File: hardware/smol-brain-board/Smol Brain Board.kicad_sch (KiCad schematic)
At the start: 67 parts, among them J1 USB4085-GF-A, J12 Jumper 2Way Vert Solderable, J3 CAN_DBG, J5 Jumper 2Way Vert Solderable, J6 Smol_Brain_Board, J7 PROGRAM, J8 Jumper 2Way Vert Solderable, J9 Jumper 2Way Vert Solderable, U1 ESP32-S3-WROOM-1-N8, U3 SN65HVD231D

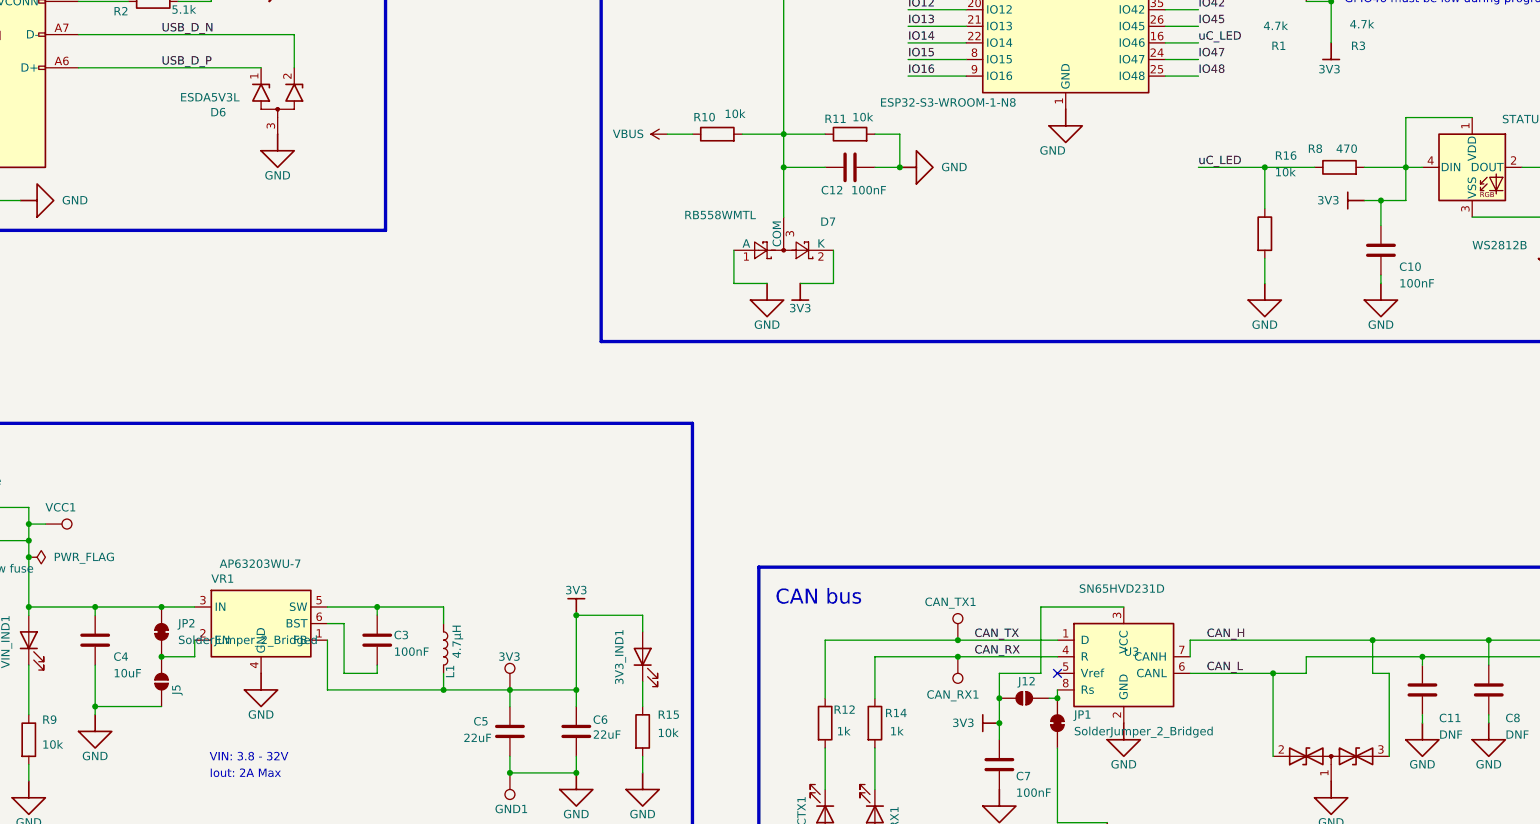
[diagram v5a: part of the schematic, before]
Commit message: Schematic fixes, foot print and crossovers, continued routing
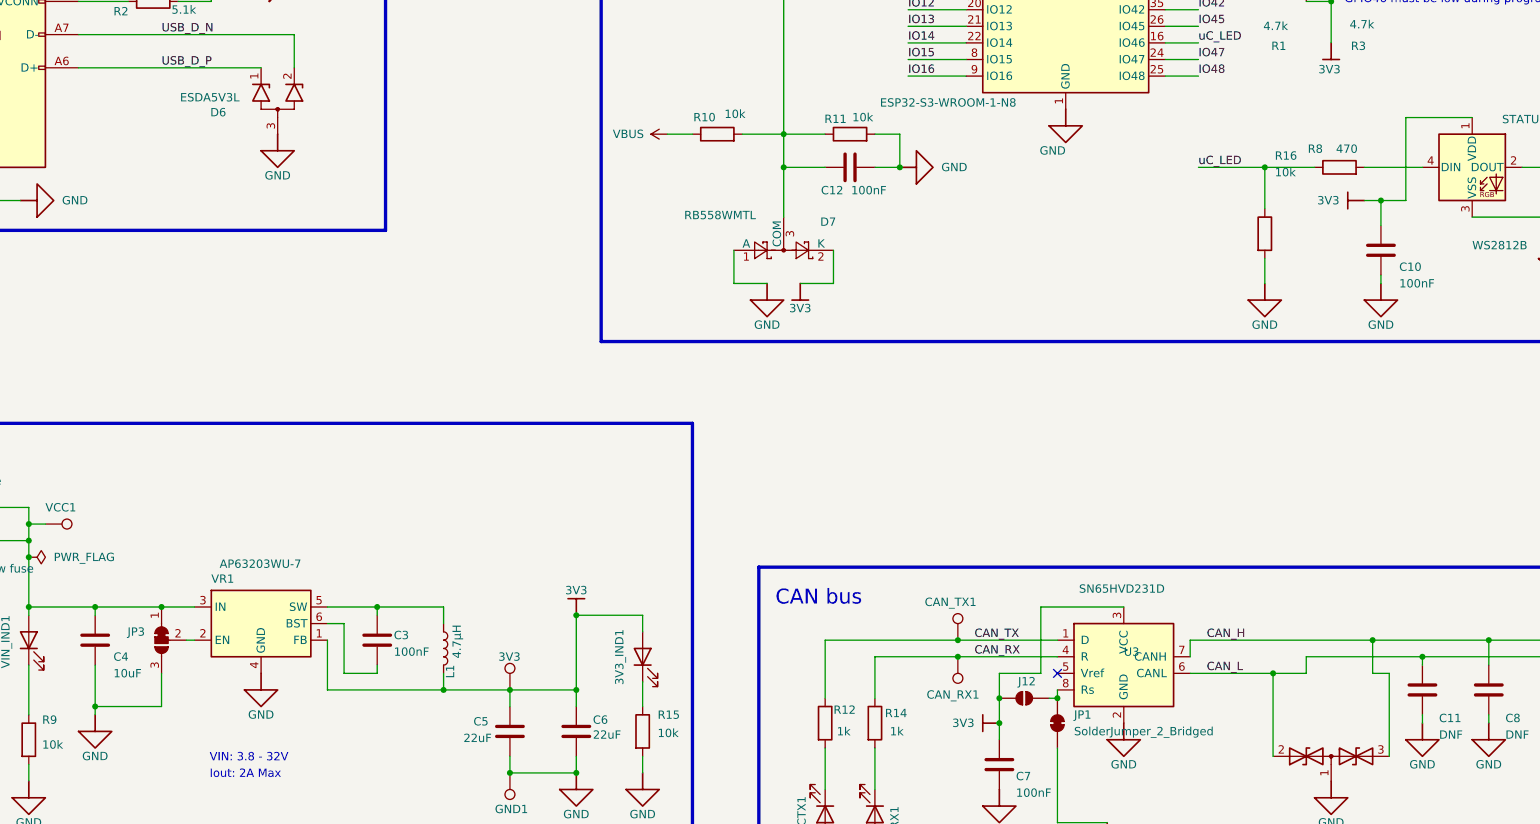
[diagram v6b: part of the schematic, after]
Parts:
- removed J5: Jumper 2Way Vert Solderable, Jumper:SolderJumper-2_P1.3mm_Bridged_RoundedPad1.0x1.5mm, symbol Jumper:SolderJumper_2_Open
- removed JP2: SolderJumper_2_Bridged, Jumper:SolderJumper-2_P1.3mm_Bridged_RoundedPad1.0x1.5mm, symbol Jumper:SolderJumper_2_Bridged
- added JP3: SolderJumper_3_Bridged12, Jumper:SolderJumper-3_P1.3mm_Bridged12_RoundedPad1.0x1.5mm, symbol Jumper:SolderJumper_3_Bridged12
- J7: footprint Connector_PinHeader_1.00mm:PinHeader_1x05_P1.00mm_Vertical -> Connector_PinHeader_2.54mm:PinHeader_1x05_P2.54mm_Vertical
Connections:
- net 3V3: no longer R8.2, STATUS1.4 (DIN)
- net GND: now also JP3.3 (B)
- net at C4.1, F1.1, F2.2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: now also JP3.1 (A)
- net at VR1.2 (EN): now also JP3.2 (C)
- new net: R8.2, STATUS1.4 (DIN)
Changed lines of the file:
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@@
 	)
 	(junction
-		(at 168.91 170.18)
+		(at 158.75 162.56)
 		(diameter 0)
 		(color 0 0 0 0)
 	)
 	(junction
-		(at 158.75 162.56)
+		(at 36.83 243.84)
 		(diameter 0)
 		(color 0 0 0 0)
 	)
 	(junction
-		(at 36.83 243.84)
+		(at 168.91 162.56)
 		(diameter 0)
 		(color 0 0 0 0)
@@
 	)
 	(junction
-		(at 359.41 95.25)
-		(diameter 0)
-		(color 0 0 0 0)
-	)
-	(junction
 		(at 36.83 80.01)
 		(diameter 0)
@@
 	)
 	(junction
-		(at 168.91 162.56)
-		(diameter 0)
-		(color 0 0 0 0)
-	)
-	(junction
 		(at 232.41 187.96)
 		(diameter 0)
@@
 	(wire
 		(pts
-			(xy 359.41 95.25) (xy 359.41 100.33)
-		)
-		(stroke
-			(width 0)
-			(type default)
-		)
-	)
-	(wire
-		(pts
-			(xy 158.75 162.56) (xy 168.91 162.56)
-		)
-		(stroke
-			(width 0)
-			(type default)
-		)
-	)
-	(wire
-		(pts
 			(xy 303.53 162.56) (xy 303.53 172.72)
 		)
@@
 	(wire
 		(pts
-			(xy 353.06 95.25) (xy 359.41 95.25)
+			(xy 353.06 95.25) (xy 361.95 95.25)
 		)
 		(stroke
@@
 	(wire
 		(pts
-			(xy 33.02 52.07) (xy 36.83 52.07)
+			(xy 168.91 172.72) (xy 168.91 177.8)
 		)
 		(stroke
@@
 	(wire
 		(pts
-			(xy 67.31 187.96) (xy 77.47 187.96)
+			(xy 33.02 52.07) (xy 36.83 52.07)
 		)
 		(stroke
@@
 	(wire
 		(pts
-			(xy 322.58 60.96) (xy 327.66 60.96)
+			(xy 67.31 187.96) (xy 77.47 187.96)
 		)
 		(stroke
@@
 	(wire
 		(pts
-			(xy 344.17 69.85) (xy 347.98 69.85)
+			(xy 322.58 60.96) (xy 327.66 60.96)
 		)
 		(stroke
@@
 	(wire
 		(pts
-			(xy 359.41 100.33) (xy 355.6 100.33)
+			(xy 344.17 69.85) (xy 347.98 69.85)
 		)
 		(stroke
@@
 	(wire
 		(pts
-			(xy 36.83 201.93) (xy 36.83 205.74)
+			(xy 359.41 100.33) (xy 355.6 100.33)
 		)
 		(stroke
@@
 	(wire
 		(pts
-			(xy 173.99 170.18) (xy 168.91 170.18)
+			(xy 36.83 201.93) (xy 36.83 205.74)
 		)
 		(stroke
@@
 	(wire
 		(pts
-			(xy 173.99 167.64) (xy 173.99 170.18)
-		)
-		(stroke
-			(width 0)
-			(type default)
-		)
-	)
-	(wire
-		(pts
 			(xy 222.25 187.96) (xy 232.41 187.96)
 		)
@@
 	(wire
 		(pts
+			(xy 168.91 162.56) (xy 173.99 162.56)
+		)
+		(stroke
+			(width 0)
+			(type default)
+		)
+	)
+	(wire
+		(pts
 			(xy 290.83 170.18) (xy 306.07 170.18)
 		)
@@
 	(wire
 		(pts
+			(xy 172.72 167.64) (xy 173.99 167.64)
+		)
+		(stroke
+			(width 0)
+			(type default)
+		)
+	)
+	(wire
+		(pts
 			(xy 33.02 67.31) (xy 36.83 67.31)
 		)
@@
 	(wire
 		(pts
-			(xy 168.91 162.56) (xy 173.99 162.56)
+			(xy 158.75 162.56) (xy 168.91 162.56)
 		)
 		(stroke
@@
 	(wire
 		(pts
-			(xy 361.95 95.25) (xy 359.41 95.25)
-		)
-		(stroke
-			(width 0)
-			(type default)
-		)
-	)
-	(wire
-		(pts
 			(xy 111.76 152.4) (xy 114.3 152.4)
 		)
@@
 	(wire
 		(pts
-			(xy 359.41 87.63) (xy 359.41 95.25)
+			(xy 359.41 87.63) (xy 359.41 100.33)
 		)
 		(stroke
@@
 	)
 	(symbol
-		(lib_id "Jumper:SolderJumper_2_Bridged")
-		(at 168.91 166.37 90)
-		(unit 1)
-		(exclude_from_sim no)
-		(in_bom no)
-		(on_board yes)
-		(dnp no)
-		(fields_autoplaced yes)
-		(property "Reference" "JP2"
-			(at 171.45 165.0999 90)
-			(effects
-				(font
-					(size 1.27 1.27)
-				)
-				(justify right)
-			)
-		)
-		(property "Value" "SolderJumper_2_Bridged"
-			(at 171.45 167.6399 90)
-			(effects
-				(font
-					(size 1.27 1.27)
-				)
-				(justify right)
-			)
-		)
-		(property "Footprint" "Jumper:SolderJumper-2_P1.3mm_Bridged_RoundedPad1.0x1.5mm"
-			(at 168.91 166.37 0)
-			(effects
-				(font
-					(size 1.27 1.27)
-				)
-				(hide yes)
-			)
-		)
-		(property "Datasheet" "~"
-			(at 168.91 166.37 0)
-			(effects
-				(font
-					(size 1.27 1.27)
-				)
-				(hide yes)
-			)
-		)
-		(property "Description" "Solder Jumper, 2-pole, closed/bridged"
-			(at 168.91 166.37 0)
-			(effects
-				(font
-					(size 1.27 1.27)
-				)
-				(hide yes)
-			)
-		)
-		(pin "2"
-		)
-		(pin "1"
-		)
-		(instances
-			(project ""
-				(path "/d947cca5-df2f-4130-8179-c021102beaa2"
-					(reference "JP2")
-					(unit 1)
-				)
-			)
-		)
-	)
-	(symbol
 		(lib_id "Smol Brain Board-altium-import:GND_SIGNAL_GROUND")
 		(at 82.55 87.63 0)
@@
 			)
 		)
-		(property "Footprint" "Connector_PinHeader_1.00mm:PinHeader_1x05_P1.00mm_Vertical"
+		(property "Footprint" "Connector_PinHeader_2.54mm:PinHeader_1x05_P2.54mm_Vertical"
 			(at 82.55 185.42 0)
 			(effects
@@
 	)
 	(symbol
-		(lib_id "Jumper:SolderJumper_2_Open")
-		(at 168.91 173.99 90)
-		(unit 1)
-		(exclude_from_sim no)
-		(in_bom no)
-		(on_board yes)
-		(dnp no)
-		(property "Reference" "J5"
-			(at 171.958 176.022 0)
-			(effects
-				(font
-					(size 1.27 1.27)
-				)
-				(justify left bottom)
-			)
-		)
-		(property "Value" "Jumper 2Way Vert Solderable"
-			(at 160.782 175.26 0)
-			(effects
-				(font
-					(size 1.27 1.27)
-				)
-				(justify left bottom)
-				(hide yes)
-			)
-		)
-		(property "Footprint" "Jumper:SolderJumper-2_P1.3mm_Bridged_RoundedPad1.0x1.5mm"
-			(at 168.91 173.99 0)
-			(effects
-				(font
-					(size 1.27 1.27)
-				)
-				(hide yes)
-			)
-		)
-		(property "Datasheet" "~"
-			(at 168.91 173.99 0)
-			(effects
-				(font
-					(size 1.27 1.27)
-				)
-				(hide yes)
-			)
-		)
-		(property "Description" "Solder Jumper, 2-pole, open"
-			(at 168.91 173.99 0)
-			(effects
-				(font
-					(size 1.27 1.27)
-				)
-				(hide yes)
-			)
-		)
-		(property "SOURCE" "QUTMS_JumperLibrary.SchLib"
-			(at 160.782 175.26 0)
-			(effects
-				(font
-					(size 1.27 1.27)
-				)
-				(justify left bottom)
-				(hide yes)
-			)
-		)
-		(property "DESIGN ITEM ID" "Jumper 2Way Vert Solderable"
-			(at 160.782 175.26 0)
-			(effects
-				(font
-					(size 1.27 1.27)
-				)
-				(justify left bottom)
-				(hide yes)
-			)
-		)
-		(pin "1"
-		)
-		(pin "2"
-		)
-		(instances
-			(project ""
-				(path "/d947cca5-df2f-4130-8179-c021102beaa2"
-					(reference "J5")
-					(unit 1)
-				)
-			)
-		)
-	)
-	(symbol
 		(lib_id "Device:R")
 		(at 336.55 31.75 270)
@@
 					(unit 1)
 				)
+			)
+		)
+	)
+	(symbol
+		(lib_id "Jumper:SolderJumper_3_Bridged12")
+		(at 168.91 167.64 90)
+		(mirror x)
+		(unit 1)
+		(exclude_from_sim no)
+		(in_bom no)
+		(on_board yes)
+		(dnp no)
+		(property "Reference" "JP3"
+			(at 166.37 166.3699 90)
+			(effects
+				(font
+					(size 1.27 1.27)
+				)
+				(justify left)
+			)
+		)
+		(property "Value" "SolderJumper_3_Bridged12"
+			(at 166.37 168.9099 90)
+			(effects
+				(font
+					(size 1.27 1.27)
+				)
+				(justify left)
+				(hide yes)
+			)
+		)
+		(property "Footprint" "Jumper:SolderJumper-3_P1.3mm_Bridged12_RoundedPad1.0x1.5mm"
+			(at 168.91 167.64 0)
+			(effects
+				(font
+					(size 1.27 1.27)
+				)
+				(hide yes)
+			)
+		)
+		(property "Datasheet" "~"
+			(at 168.91 167.64 0)
+			(effects
+				(font
+					(size 1.27 1.27)
+				)
+				(hide yes)
+			)
+		)
+		(property "Description" "3-pole Solder Jumper, pins 1+2 closed/bridged"
+			(at 168.91 167.64 0)
+			(effects
+				(font
+					(size 1.27 1.27)
+				)
+				(hide yes)
+			)
+		)
+		(pin "2"
+		)
+		(pin "3"
+		)
+		(pin "1"
+		)
+		(instances
+			(project ""
+				(path "/d947cca5-df2f-4130-8179-c021102beaa2"
+					(reference "JP3")
+					(unit 1)
+				)

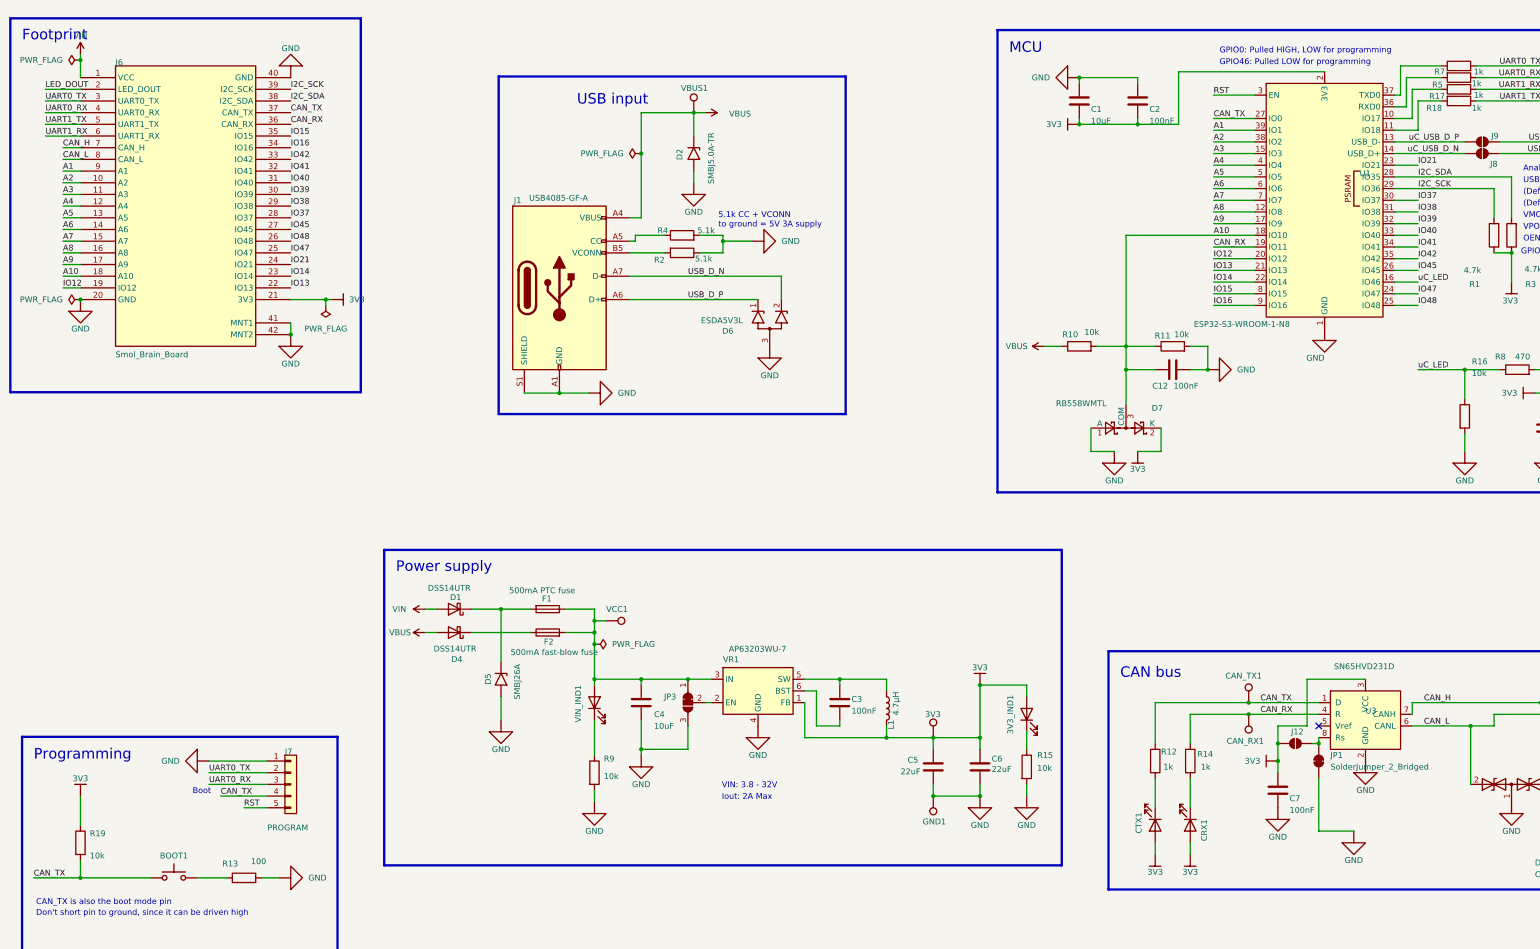
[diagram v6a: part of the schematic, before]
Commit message: Impedence matching USB data
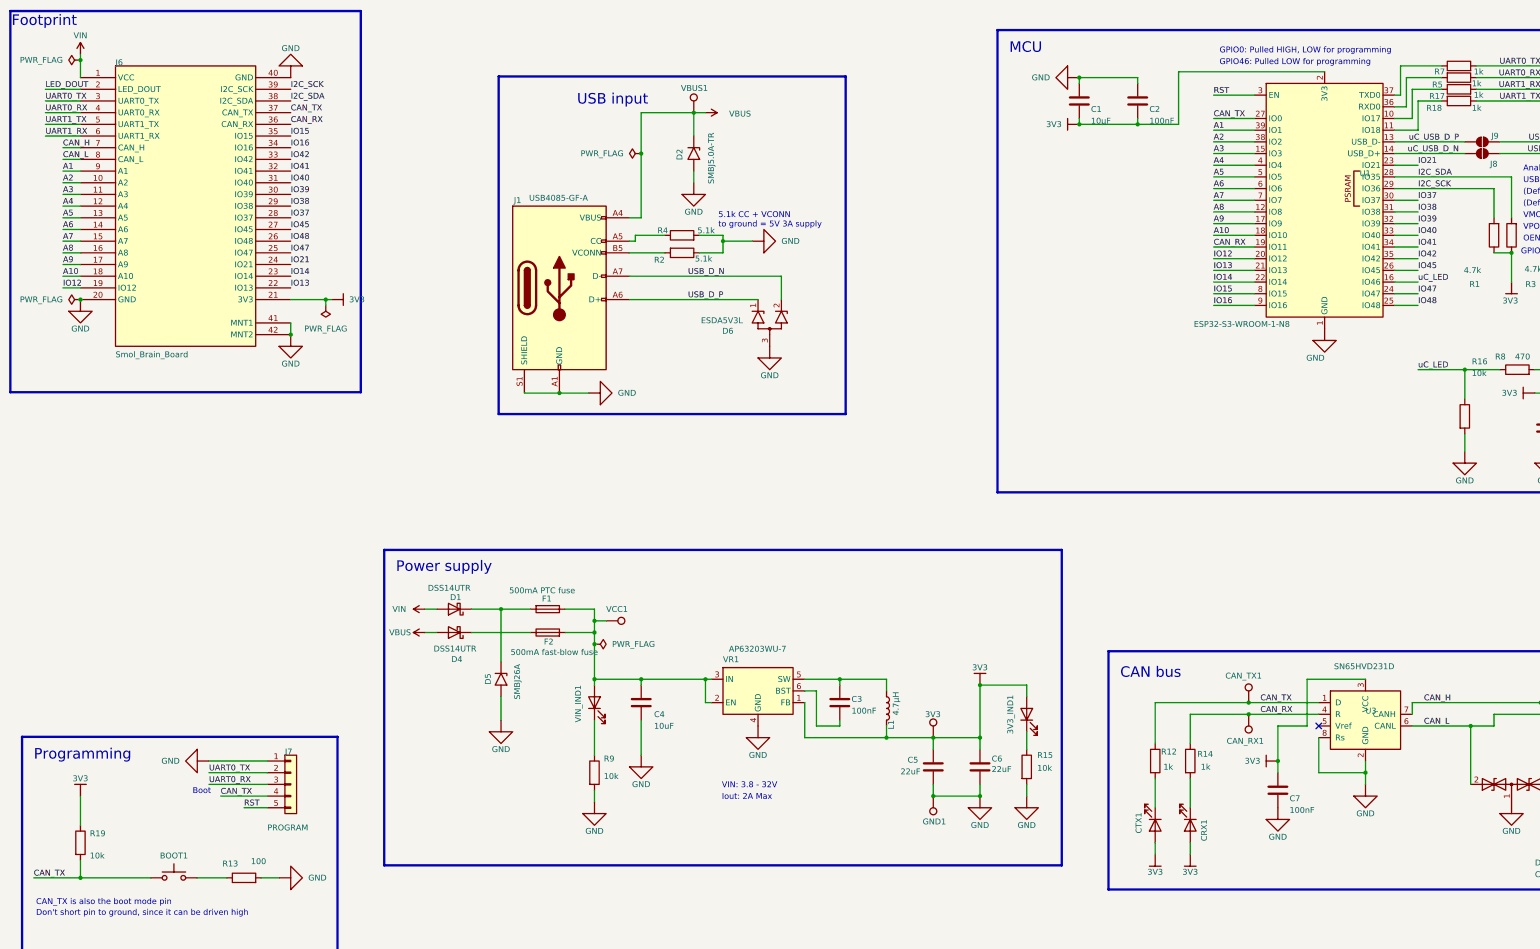
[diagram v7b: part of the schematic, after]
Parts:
- removed C12: Capacitor 100n 50V 0603, Capacitor_SMD:C_0603_1608Metric, symbol Device:C
- removed D7: RB558WMTL, Package_TO_SOT_SMD:SOT-416, symbol Diode:BAT54S
- removed J12: Jumper 2Way Vert Solderable, Jumper:SolderJumper-2_P1.3mm_Open_RoundedPad1.0x1.5mm, symbol Jumper:SolderJumper_2_Open
- removed JP1: SolderJumper_2_Bridged, Jumper:SolderJumper-2_P1.3mm_Bridged_RoundedPad1.0x1.5mm, symbol Jumper:SolderJumper_2_Bridged
- removed JP3: SolderJumper_3_Bridged12, Jumper:SolderJumper-3_P1.3mm_Bridged12_RoundedPad1.0x1.5mm, symbol Jumper:SolderJumper_3_Bridged12
- removed R10, R11: Resistor 10k 0603, Resistor_SMD:R_0201_0603Metric, symbol Device:R
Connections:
- net GND: now also U3.8 (Rs)
- net at C4.1, F1.1, F2.2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: now also VR1.2 (EN)

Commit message: Routing complete, DRC passing, inspection required
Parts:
- J6: footprint (none) -> Library:Smol_Brain_Board; symbol QUTRC ARC:root_0_Smol_Brain_Board_QUTRC ARC -> smol_brain_board:Smol_Brain_Board; now left out of the parts list
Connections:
- net GND: no longer J6.41 (MNT1), J6.42 (MNT2)
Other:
- note removed: "James Nichol, Brock Morgan, Maurice Blake"
- company: (none) -> QUT Robotics Club
